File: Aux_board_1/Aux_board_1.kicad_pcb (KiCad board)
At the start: 2 copper layers, 60 parts, among them J1 P03d, J2 P11a, J3 P10a, J4 PHI_ENC, J5 PHI_LIM_CLW, J6 PHI_LIM_CCW, J7 PHI_HOME, Q1 BSS138, Q10 BSS84, Q2 BSS84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

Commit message: Finished routing board 1
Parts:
- moved R30 129.8 mm to (140.9, 114.9), turned to 90 degrees
- moved R27 129.2 mm to (141.0, 103.4), turned to 90 degrees
- moved R29 126.1 mm to (145.5, 114.9), turned to 90 degrees
- moved R26 125.4 mm to (145.5, 103.4), turned to 90 degrees
- moved R28 122.6 mm to (150.1, 114.9), turned to 90 degrees
- moved R25 121.8 mm to (150.1, 103.4), turned to 90 degrees
- moved R18 107.4 mm to (154.7, 114.9), turned to 90 degrees
- moved R15 106.6 mm to (154.7, 103.4), turned to 90 degrees
- moved R16 99.1 mm to (165.6, 114.9), turned to 90 degrees
- moved R13 98.1 mm to (165.6, 103.4), turned to 90 degrees
- moved Q10 93.2 mm to (160.1, 114.9), turned to -90 degrees
- moved Q8 93.0 mm to (160.1, 103.4), turned to -90 degrees
- moved R17 88.0 mm to (176.4, 114.9), turned to -90 degrees
- moved R14 86.9 mm to (176.4, 103.4), turned to -90 degrees
- moved R24 83.6 mm to (140.9, 92.4), turned to 90 degrees
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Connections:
- U1 pad 7: unconnected-(U1-Vout+-Pad7) -> +5V
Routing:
- net +24V: track 0.00 -> 459.7 mm, vias 0 -> 8
- net +5V: track 0.00 -> 138.3 mm, vias 0 -> 5
- net /PHI_ENC_B: track 0.00 -> 136.4 mm, vias 0 -> 3
- net /TH_HOME: track 0.00 -> 132.3 mm
- net /R_HOME: track 0.00 -> 130.2 mm, vias 0 -> 2
- net GND: track 0.00 -> 130.1 mm, vias 0 -> 11
- net /PHI_LIM_CCW: track 0.00 -> 128.4 mm, vias 0 -> 2
- net /PHI_LIM_CLW: track 0.00 -> 127.0 mm, vias 0 -> 2
- net /PHI_HOME: track 0.00 -> 125.8 mm, vias 0 -> 1
- net /R_LIM_MAX: track 0.00 -> 122.4 mm
- net /TH_LIM_CLW: track 0.00 -> 118.9 mm, vias 0 -> 2
- net /PHI_ENC_A: track 0.00 -> 118.2 mm, vias 0 -> 3
- net /ALF_LIM_2: track 0.00 -> 117.8 mm, vias 0 -> 2
- net /BET_LIM_2: track 0.00 -> 116.8 mm, vias 0 -> 2
- net /R_LIM_MIN: track 0.00 -> 113.7 mm
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
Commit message: finished designing Board 1
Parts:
- added MH1: MountingHole_3mm, MountingHole:MountingHole_3mm, F.Cu at (55.0, 53.2)
- added MH2: MountingHole_3mm, MountingHole:MountingHole_3mm, F.Cu at (171.5, 53.2)
- added MH3: MountingHole_3mm, MountingHole:MountingHole_3mm, F.Cu at (55.0, 126.5)
- added MH4: MountingHole_3mm, MountingHole:MountingHole_3mm, F.Cu at (171.5, 126.5)
- added REF**: INDACTlogo, LEGOkor:INDACTlogo, F.Cu at (79.9, 85.7)
- added REF**: LEGOkorLogo, LEGOkor:LEGOkorLogo, F.Cu at (117.6, 77.3)
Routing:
- net +24V: track 459.7 -> 454.8 mm
- net GND: track 130.1 -> 134.8 mm, vias 11 -> 150
- net +5V: track 138.3 -> 139.5 mm
- added copper zone on B.Cu, net GND
- added copper zone on F.Cu, net GND
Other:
- board outline added: 153 x 83.5 mm
- board text added: "+24V"
- board text added: "+3.3V"
- board text added: "+5V"
- board text added: "24V to 5V buck converter"
- board text added: "3V3 5V 24V"
- board text added: "GND"
- board text added: "GND B A V+"
- board text added: "GND LIM V+"
- board text added: "GND SNS V+"
- board text added: "Karcsi - Aux. Board 1"
- board text added: "LDO"
- board text added: "P10a TO AUX. BOARD 2"
- board text added: "P11a TO AUX. BOARD 3"
- board text added: "P4d TO MAIN BOARD"
- board text added: "PHI ENCODER"
- board text added: "PHI HOME SNS."
- board text added: "PHI LIM.SW. ↶"
- board text added: "PHI LIM.SW. ↷"
- board text added: "Rev 1.0"
- board text added: "Select supply voltage with 0R resistors"

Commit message: Finished Board 2 schematic
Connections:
- net /PHIL_LIM_CLW_IN renamed /PHI_LIM_CLW_IN

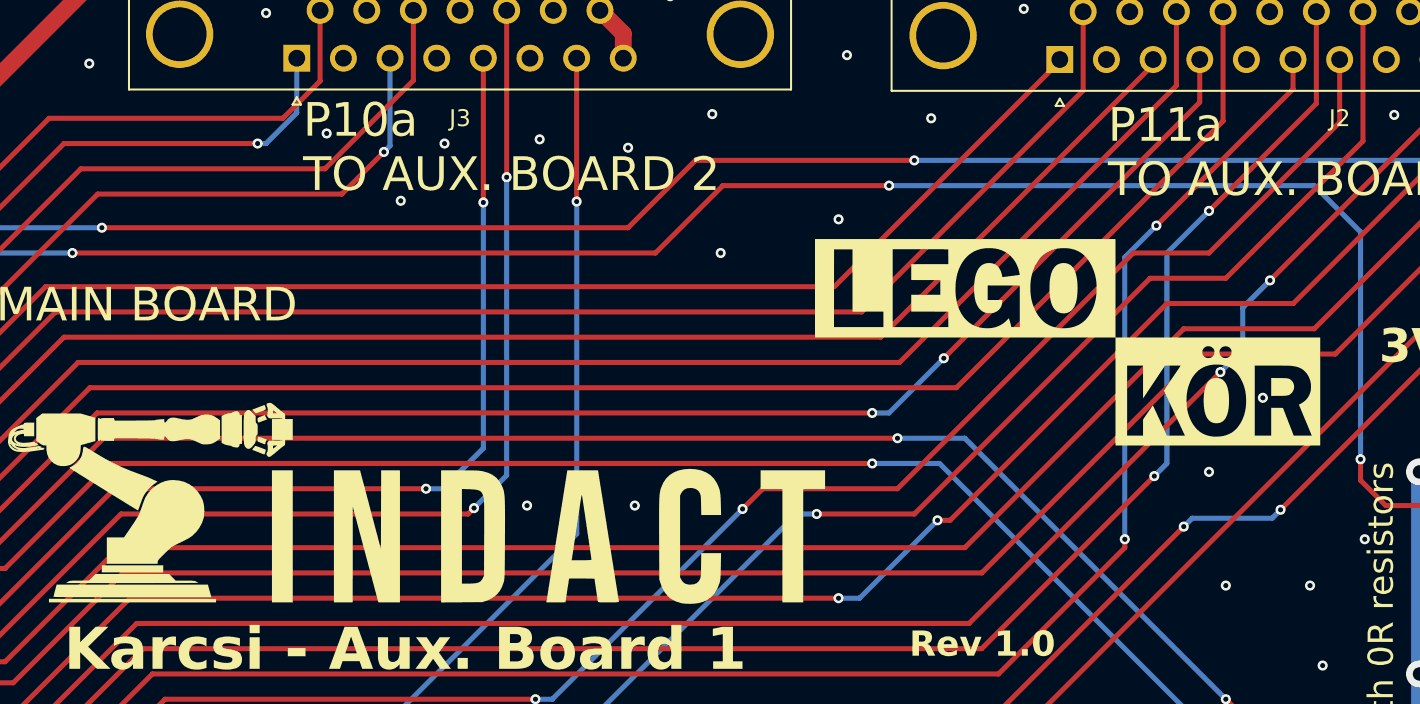
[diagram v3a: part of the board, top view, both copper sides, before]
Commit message: Started placement&routing Board 2
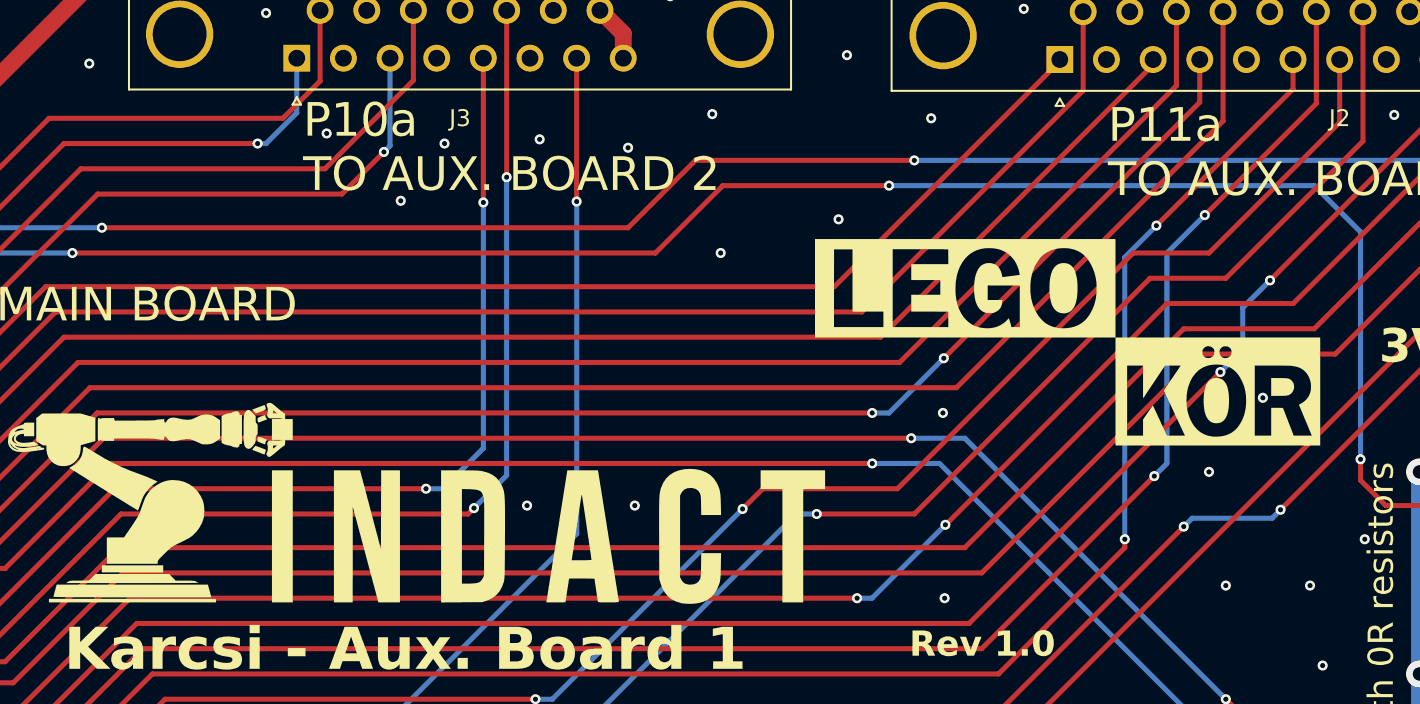
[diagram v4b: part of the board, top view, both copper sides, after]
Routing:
- net GND: vias 150 -> 152
